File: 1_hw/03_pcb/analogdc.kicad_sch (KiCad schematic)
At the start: 0 parts

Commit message: FEAT: Added Analog Stage 2 to Schematic. Some additional symbols (Pot, SPDT Analog MUX, etc.) added to Project.
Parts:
- added C? (x4): 100n, Capacitor_SMD:C_0603_1608Metric, symbol Device:C_Small
- added R?: 10k, Resistor_SMD:R_0603_1608Metric, symbol Device:R_Small_US
- added R? (x4): 499, symbol Device:R_Small_US
- added R?: 0, Resistor_SMD:R_0603_1608Metric, symbol Device:R_Small_US
- added U?: LM6171D, Package_SO:SOIC-8_3.9x4.9mm_P1.27mm, symbol BRZK_OPAMP:LM6171D
- added U?: TMUX6104, TBD, symbol BRZK_MUX:TMUX6104
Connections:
- new net: R?.2, R?.2, U?.2 (-)
- new net: R?.1, R?.2, U?.3 (+)
- new net: R?.1, R?.2, U?.6
- new net: R?.2, U?.5 (S2)
- new net: U?.7 (NC), U?.8 (NC), U?.9 (NC)
- new net 15P0V_A: C?.1, C?.1, U?.13 (VDD), U?.7 (V+)
- new net 3P3V_A: R?.1
- new net ANALOG_DAC2_MCU_AMUX3: R?.1, U?.4 (S1)
- new net ANALOG_DC-OFFSET_AMUX3_AMP3: U?.6 (D)
- new net GND_A: C?.2, C?.2, C?.2, C?.2, R?.1, U?.11 (S3), U?.14 (A1)
- new net GND_D: R?.1
- new net GPIO_EN_MCU_AMUX3_3P3: R?.2, U?.2 (EN)
- new net GPIO_SEL0_MCU_AMUX3_3P3: U?.1 (A0)
- new net GPIO_SEL1_MCU_AMUX3_3P3: U?.14 (A1)
- new net N15P0V_A: C?.1, C?.1, U?.3 (VSS), U?.4 (V-)
- no-connect marks 0 -> 1
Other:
- note added: "ANALOG MUX #3 DC OFFSET SELECT"

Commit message: FEAT: Changed from two grounds (Digital + Analog) to Singular Ground IAW recommended Grounding Scheme.
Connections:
- net GND_D is gone; now on net GND: R?.1
- net GND_A renamed GND
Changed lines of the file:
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@@
 			)
 		)
-		(property "Value" "GND_A"
+		(property "Value" "GND"
 			(at 208.026 119.634 0)
 			(effects
@@
 			)
 		)
-		(property "Value" "GND_A"
+		(property "Value" "GND"
 			(at 191.77 119.634 0)
 			(effects
@@
 			)
 		)
-		(property "Value" "GND_A"
+		(property "Value" "GND"
 			(at 213.36 86.36 0)
 			(effects
@@
 			)
 		)
-		(property "Value" "GND_A"
+		(property "Value" "GND"
 			(at 90.17 116.84 0)
 			(effects
@@
 			)
 		)
-		(property "Value" "GND_A"
+		(property "Value" "GND"
 			(at 109.22 121.92 0)
 			(effects
@@
 			)
 		)
-		(property "Value" "GND_D"
+		(property "Value" "GND"
 			(at 184.15 119.38 0)
 			(effects
@@
 			)
 		)
-		(property "Value" "GND_A"
+		(property "Value" "GND"
 			(at 217.17 127 0)
 			(effects
@@
 			)
 		)
-		(property "Value" "GND_A"
+		(property "Value" "GND"
 			(at 107.95 96.52 0)
 			(effects

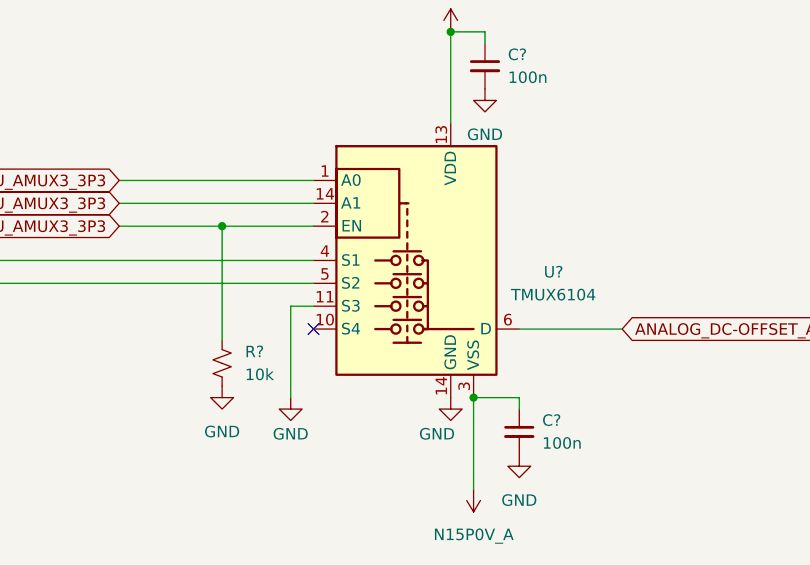
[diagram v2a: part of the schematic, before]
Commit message: FEAT: Added +15V and -15V Regulator. Replaced some Symbols to add additional Part Number Field.
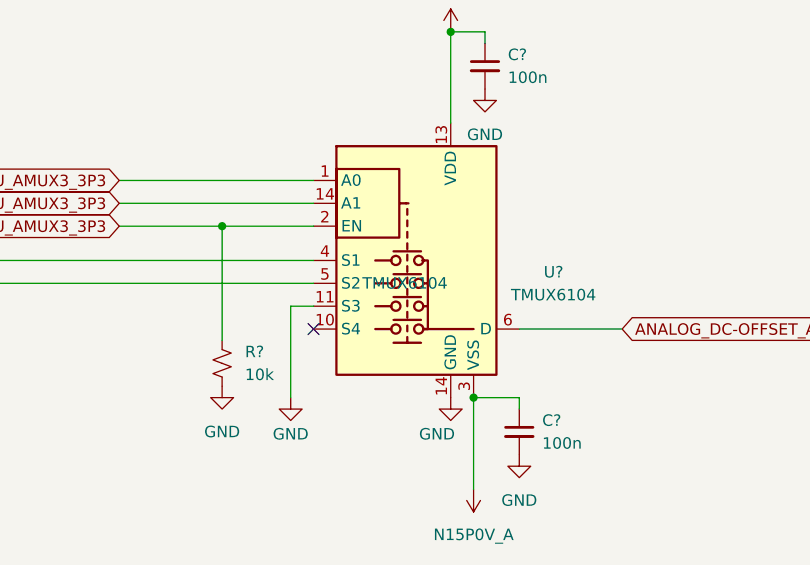
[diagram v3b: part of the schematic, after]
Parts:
- U?: Part Number (none) -> LM6171D
- U?: footprint TBD -> BRZK_TBD; Part Number (none) -> TMUX6104
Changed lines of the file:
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@@
+			)
+		)
+		(property "Part Number" "LM6171D"
+			(at 106.68 102.87 0)
+			(effects
+				(font
+					(size 1.27 1.27)
+				)
+				(hide yes)
 			)
 		)
@@
 			)
 		)
-		(property "Footprint" "TBD"
+		(property "Footprint" "BRZK_TBD"
 			(at 204.47 105.41 0)
 			(effects
@@
 			)
 		)
+		(property "Part Number" "TMUX6104"
+			(at 204.47 102.87 0)
+			(effects
+				(font
+					(size 1.27 1.27)
+				)
+			)
+		)

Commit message: FEAT: Added Clocking Sheet, FPGA Flash, and FPGA Decoupling.
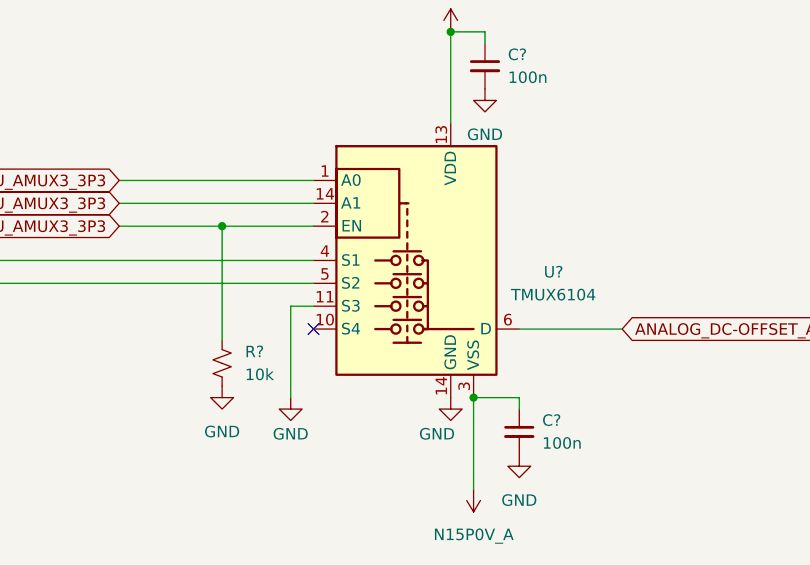
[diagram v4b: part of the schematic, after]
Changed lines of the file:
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@@
 					(size 1.27 1.27)
 				)
+				(hide yes)
 			)
 		)

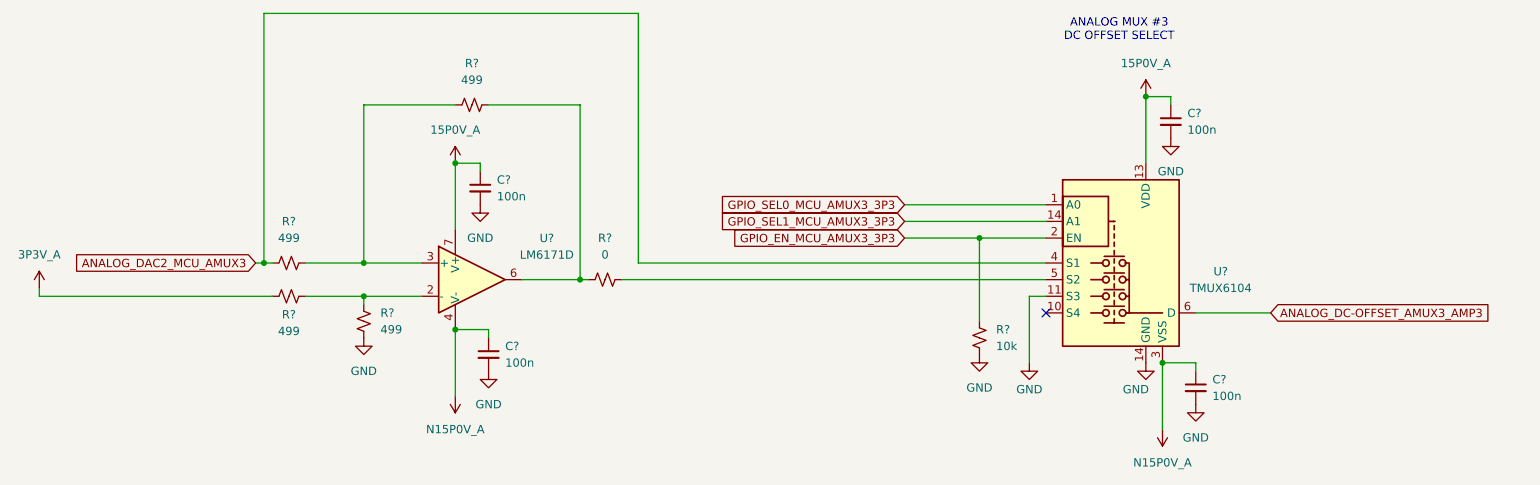
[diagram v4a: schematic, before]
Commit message: FEAT: Added Connectors on Schematic. Created Connector Footprints.
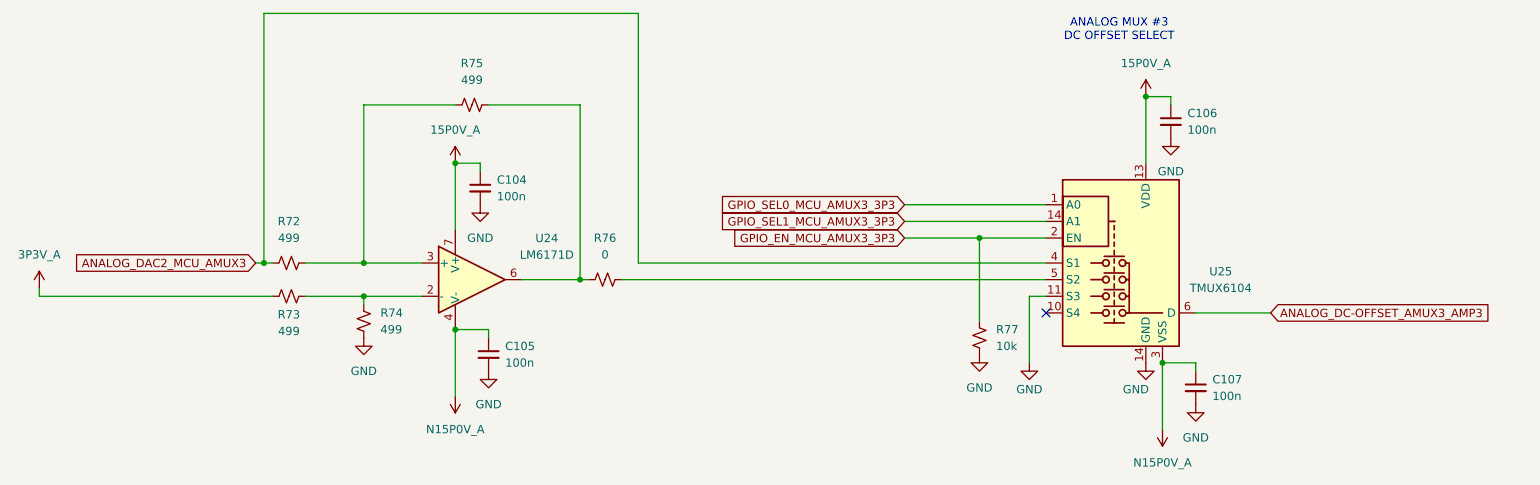
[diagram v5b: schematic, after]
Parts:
- gave numbers to parts that had none: 12
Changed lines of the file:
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@@
 		(dnp no)
 		(fields_autoplaced yes)
-		(property "Reference" "R?"
+		(property "Reference" "R77"
 			(at 186.69 110.4899 0)
 			(effects
@@
 			(project "arb"
 				(path "/866ef9be-3b01-4288-a6e0-a2357aa17e50/dd20ed2c-105a-40ef-bdba-a4198899f68e"
-					(reference "R?")
+					(reference "R77")
 					(unit 1)
 				)
@@
 		(dnp no)
 		(fields_autoplaced yes)
-		(property "Reference" "C?"
+		(property "Reference" "C105"
 			(at 111.76 113.0363 0)
 			(effects
@@
 			(project "arb"
 				(path "/866ef9be-3b01-4288-a6e0-a2357aa17e50/dd20ed2c-105a-40ef-bdba-a4198899f68e"
-					(reference "C?")
+					(reference "C105")
 					(unit 1)
 				)
@@
 		(dnp no)
 		(fields_autoplaced yes)
-		(property "Reference" "R?"
+		(property "Reference" "R74"
 			(at 92.71 107.9499 0)
 			(effects
@@
 			(project "arb"
 				(path "/866ef9be-3b01-4288-a6e0-a2357aa17e50/dd20ed2c-105a-40ef-bdba-a4198899f68e"
-					(reference "R?")
+					(reference "R74")
 					(unit 1)
 				)
@@
 		(on_board yes)
 		(dnp no)
-		(property "Reference" "R?"
+		(property "Reference" "R73"
 			(at 78.74 108.204 90)
 			(effects
@@
 			(project "arb"
 				(path "/866ef9be-3b01-4288-a6e0-a2357aa17e50/dd20ed2c-105a-40ef-bdba-a4198899f68e"
-					(reference "R?")
+					(reference "R73")
 					(unit 1)
 				)
@@
 		(dnp no)
 		(fields_autoplaced yes)
-		(property "Reference" "R?"
+		(property "Reference" "R75"
 			(at 106.68 69.85 90)
 			(effects
@@
 			(project "arb"
 				(path "/866ef9be-3b01-4288-a6e0-a2357aa17e50/dd20ed2c-105a-40ef-bdba-a4198899f68e"
-					(reference "R?")
+					(reference "R75")
 					(unit 1)
 				)
@@
 		(dnp no)
 		(fields_autoplaced yes)
-		(property "Reference" "R?"
+		(property "Reference" "R72"
 			(at 78.74 93.98 90)
 			(effects
@@
 			(project "arb"
 				(path "/866ef9be-3b01-4288-a6e0-a2357aa17e50/dd20ed2c-105a-40ef-bdba-a4198899f68e"
-					(reference "R?")
+					(reference "R72")
 					(unit 1)
 				)
@@
 		(dnp no)
 		(fields_autoplaced yes)
-		(property "Reference" "C?"
+		(property "Reference" "C107"
 			(at 219.71 118.1163 0)
 			(effects
@@
 			(project "arb"
 				(path "/866ef9be-3b01-4288-a6e0-a2357aa17e50/dd20ed2c-105a-40ef-bdba-a4198899f68e"
-					(reference "C?")
+					(reference "C107")
 					(unit 1)
 				)
@@
 		(dnp no)
 		(fields_autoplaced yes)
-		(property "Reference" "R?"
+		(property "Reference" "R76"
 			(at 127 96.52 90)
 			(effects
@@
 			(project "arb"
 				(path "/866ef9be-3b01-4288-a6e0-a2357aa17e50/dd20ed2c-105a-40ef-bdba-a4198899f68e"
-					(reference "R?")
+					(reference "R76")
 					(unit 1)
 				)
@@
 		(dnp no)
 		(fields_autoplaced yes)
-		(property "Reference" "C?"
+		(property "Reference" "C106"
 			(at 215.9 77.4763 0)
 			(effects
@@
 			(project "arb"
 				(path "/866ef9be-3b01-4288-a6e0-a2357aa17e50/dd20ed2c-105a-40ef-bdba-a4198899f68e"
-					(reference "C?")
+					(reference "C106")
 					(unit 1)
 				)
@@
 		(dnp no)
 		(fields_autoplaced yes)
-		(property "Reference" "U?"
+		(property "Reference" "U24"
 			(at 118.11 96.5514 0)
 			(effects
@@
 			(project "arb"
 				(path "/866ef9be-3b01-4288-a6e0-a2357aa17e50/dd20ed2c-105a-40ef-bdba-a4198899f68e"
-					(reference "U?")
+					(reference "U24")
 					(unit 1)
 				)
@@
 		(on_board yes)
 		(dnp no)
-		(property "Reference" "U?"
+		(property "Reference" "U25"
 			(at 220.98 101.6314 0)
 			(effects
@@
 			(project "arb"
 				(path "/866ef9be-3b01-4288-a6e0-a2357aa17e50/dd20ed2c-105a-40ef-bdba-a4198899f68e"
-					(reference "U?")
+					(reference "U25")
 					(unit 1)
 				)
@@
 		(dnp no)
 		(fields_autoplaced yes)
-		(property "Reference" "C?"
+		(property "Reference" "C104"
 			(at 110.49 87.6363 0)
 			(effects
@@
 			(project "arb"
 				(path "/866ef9be-3b01-4288-a6e0-a2357aa17e50/dd20ed2c-105a-40ef-bdba-a4198899f68e"
-					(reference "C?")
-					(unit 1)
-				)
+					(reference "C104")
+					(unit 1)
+				)

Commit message: FEAT: Assigned Reference Designators; Assigned Passives Part Numbers & Footprints (0603); Assigned LCSC P/Ns.
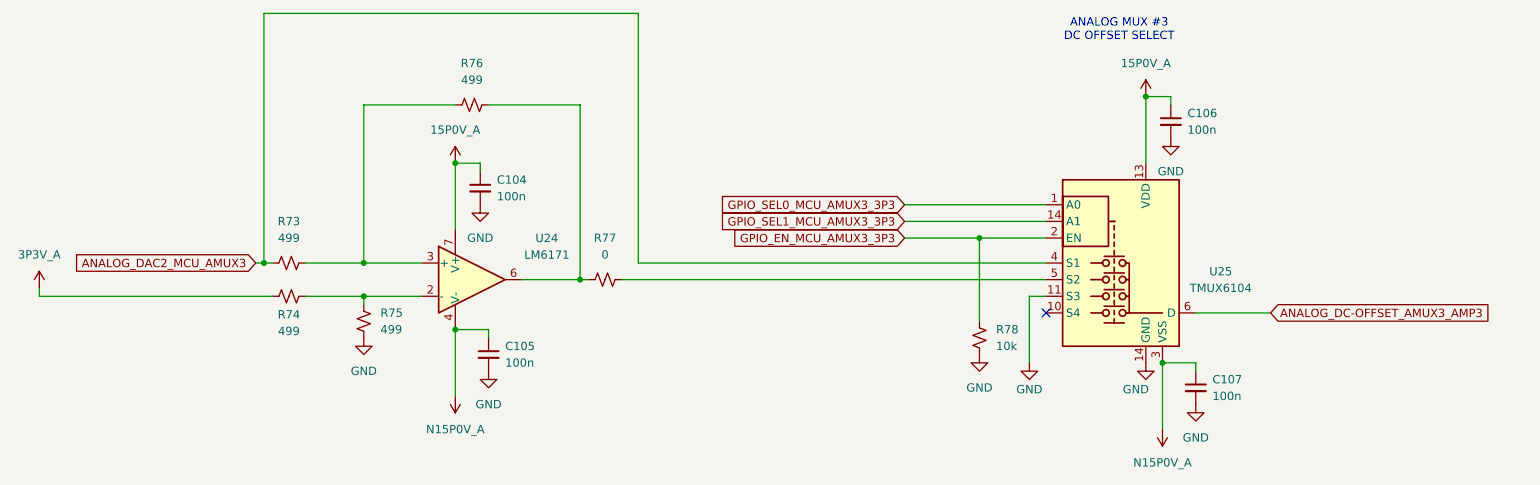
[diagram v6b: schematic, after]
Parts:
- C104, C105, C106, C107: LCSC (none) -> C24452; PN CL10B104JB8NNNC -> (none); Part Number (none) -> CL10B104JB8NNNC
- R73: renamed from R72; footprint (none) -> Resistor_SMD:R_0603_1608Metric; LCSC (none) -> C23065; Part Number (none) -> 0603WAF4990T5E
- R74: renamed from R73; footprint (none) -> Resistor_SMD:R_0603_1608Metric; LCSC (none) -> C23065; Part Number (none) -> 0603WAF4990T5E
- R75: renamed from R74; footprint (none) -> Resistor_SMD:R_0603_1608Metric; LCSC (none) -> C23065; Part Number (none) -> 0603WAF4990T5E
- R76: renamed from R75; footprint (none) -> Resistor_SMD:R_0603_1608Metric; LCSC (none) -> C23065; Part Number (none) -> 0603WAF4990T5E
- R77: renamed from R76; LCSC (none) -> C15402; PN 0603WAJ0000T5E -> (none); Part Number (none) -> 0603WAJ0000T5E
- R78: renamed from R77; LCSC (none) -> C25804; PN CR-03FC7---10K -> (none); Part Number (none) -> 0603WAF1002T5E
- U24: value LM6171D -> LM6171; symbol BRZK_OPAMP:LM6171D -> BRZK_OPAMP:LM6171; LCSC (none) -> C2058493; Part Number LM6171D -> LM6171BIMX/NOPB
- U25: footprint BRZK_TBD -> (none); LCSC (none) -> C2673388; Part Number TMUX6104 -> TMUX6104PWR
